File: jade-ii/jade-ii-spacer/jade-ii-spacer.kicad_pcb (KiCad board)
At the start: 2 copper layers, 93 x 127.3 mm, 23 parts

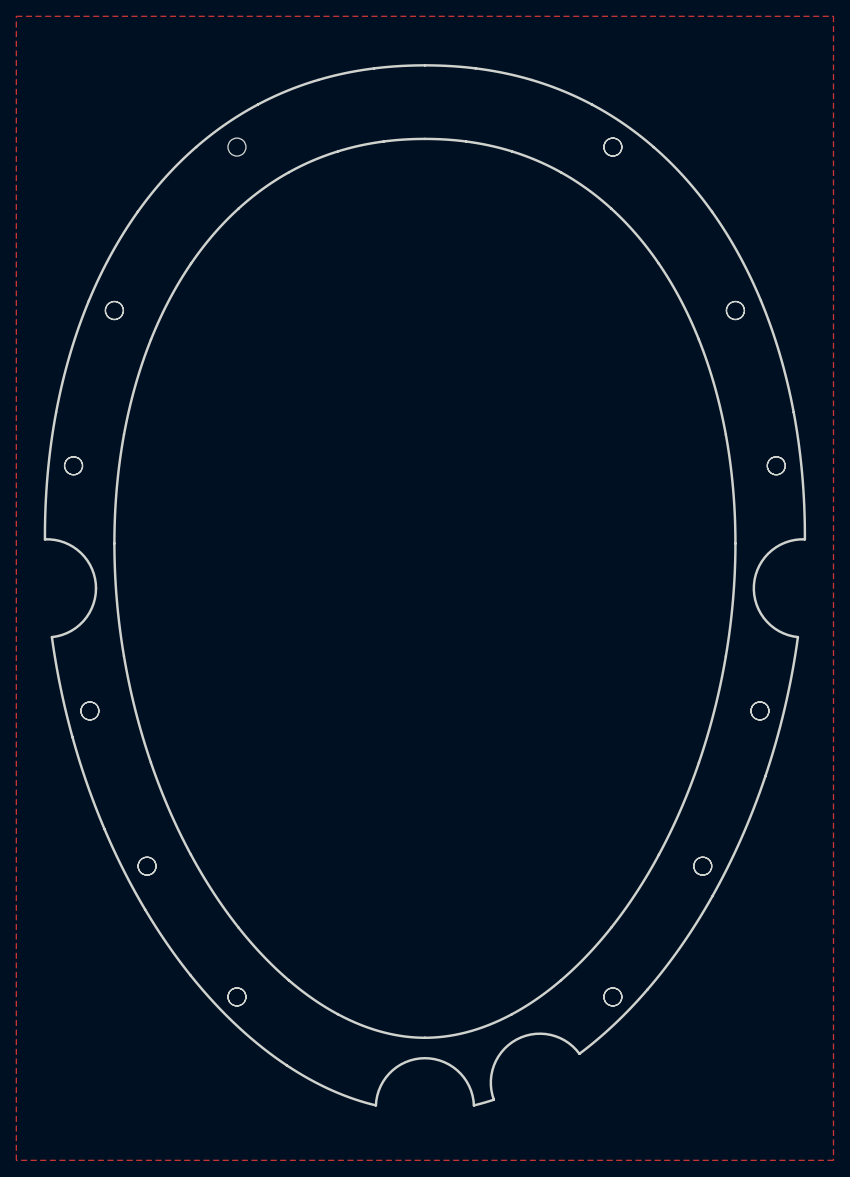
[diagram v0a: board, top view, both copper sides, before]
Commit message: jade: spacer should have 3 holes on the bottom
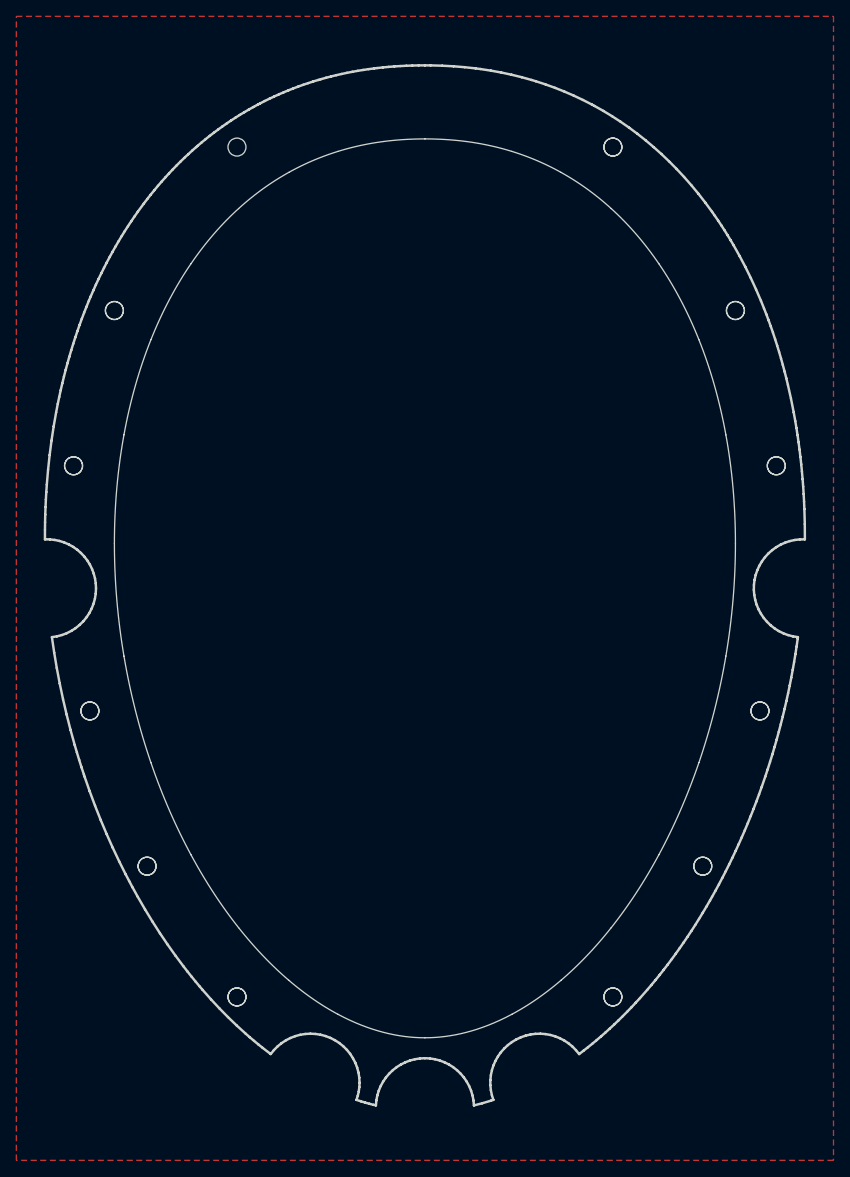
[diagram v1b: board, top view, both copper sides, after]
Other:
- outline, holes or cut-outs redrawn

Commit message: jade: remove top solder mask from spacer
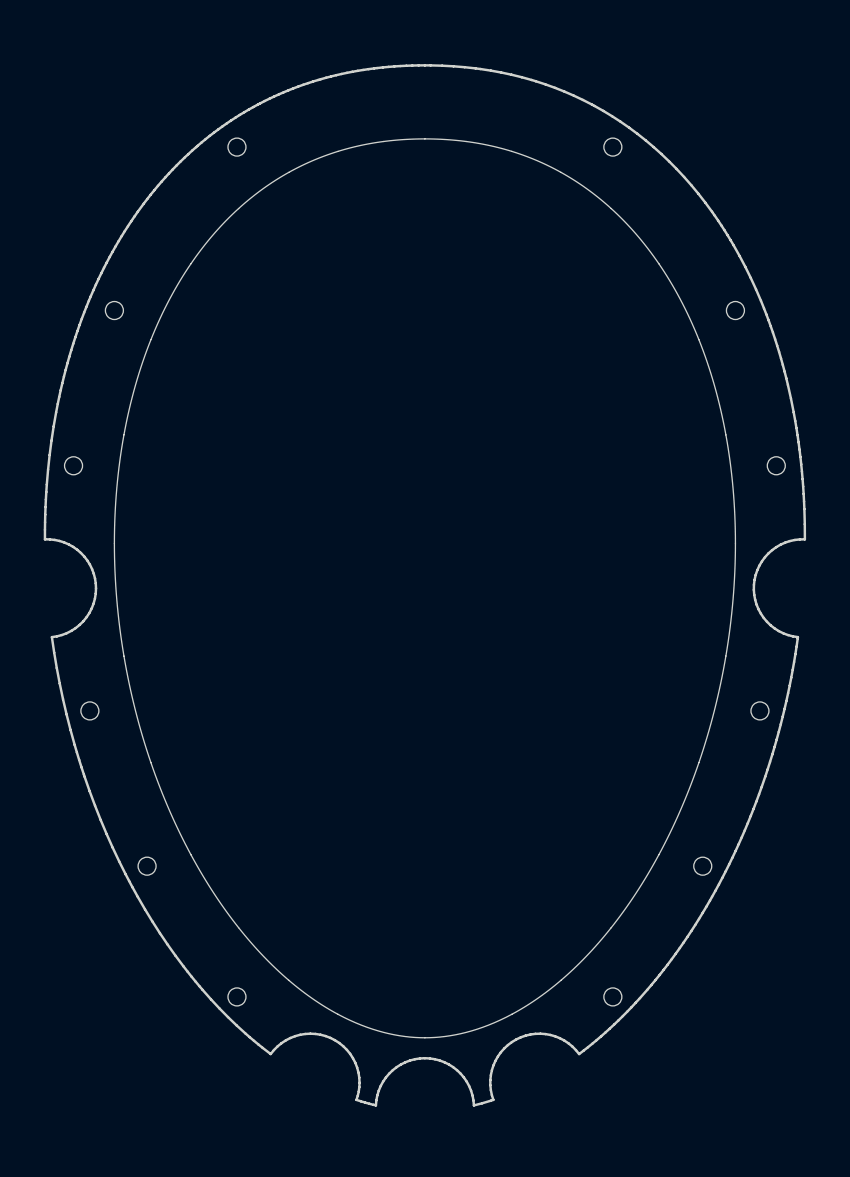
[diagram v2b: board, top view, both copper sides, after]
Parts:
- removed ? (x11): , 
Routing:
- removed copper zone on F.Cu, net (none)

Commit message: jade: i don't even know
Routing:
- added copper zone on F.Cu, net (none)
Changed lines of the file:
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@@
 		(layer "Edge.Cuts")
+	)
+	(zone
+		(net 0)
+		(net_name "")
+		(layer "F.Cu")
+		(hatch edge 0.5)
+		(connect_pads
+			(clearance 0.5)
+		)
+		(min_thickness 0.25)
+		(filled_areas_thickness no)
+		(fill yes
+			(thermal_gap 0.5)
+			(thermal_bridge_width 0.5)
+			(island_removal_mode 1)
+			(island_area_min 10)
+		)
+		(polygon
+			(pts
+				(xy -50 -70) (xy 50 -70) (xy 50 70) (xy -50 70)
+			)
+		)
 	)
 	(embedded_fonts no)

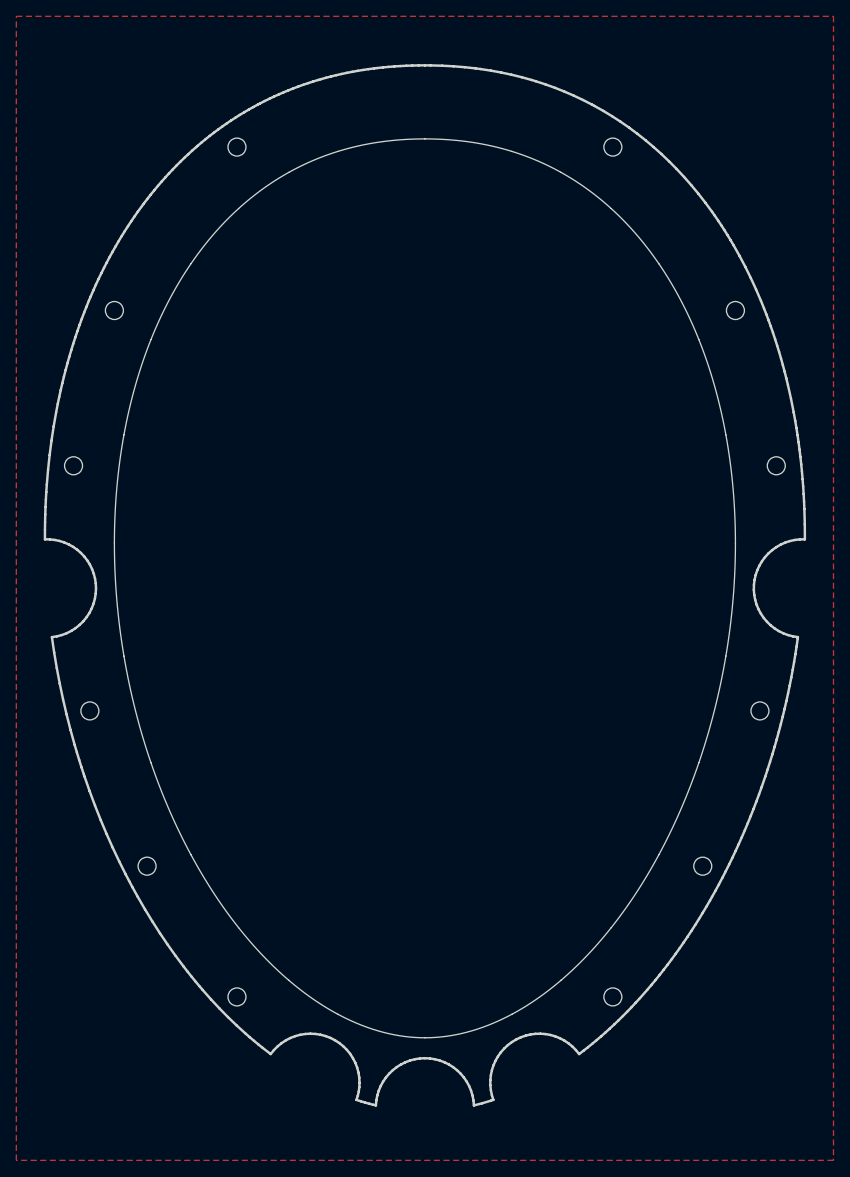
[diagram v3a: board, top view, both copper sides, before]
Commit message: jade: missing spacer cable solder point
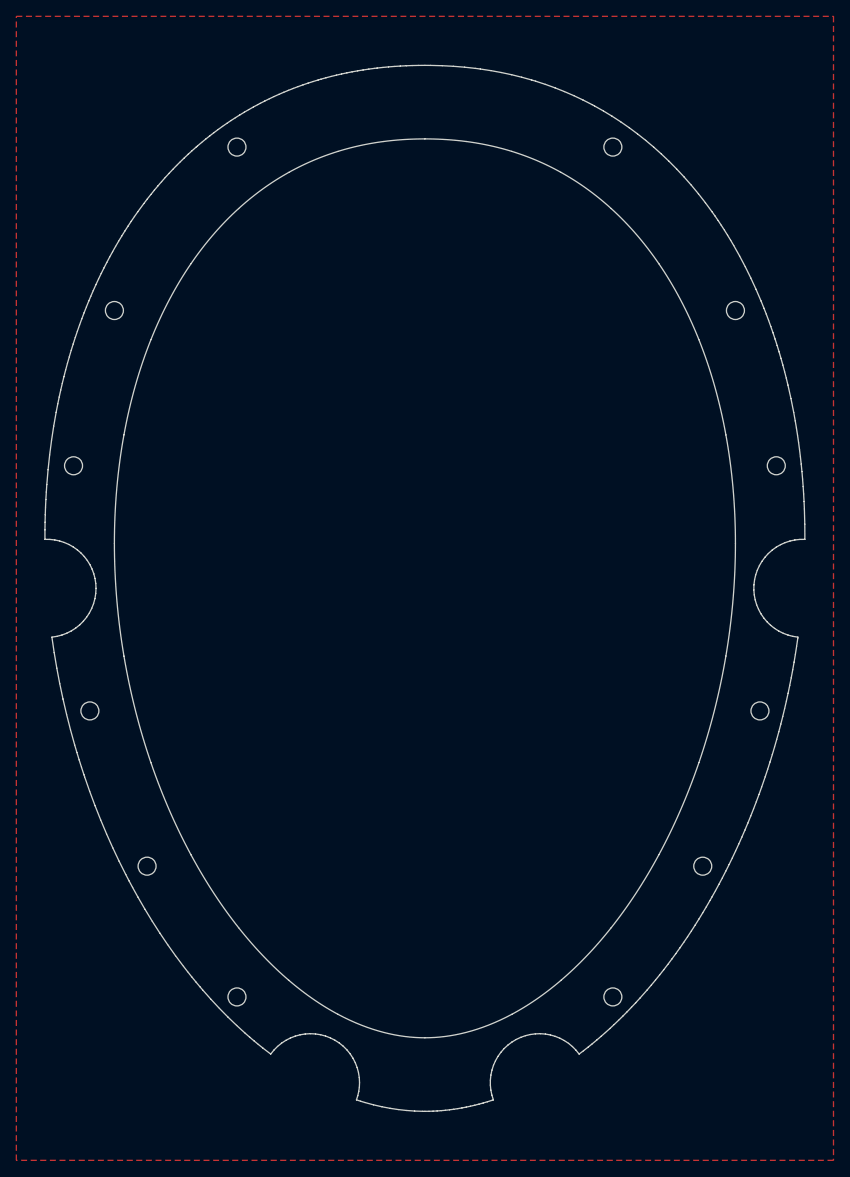
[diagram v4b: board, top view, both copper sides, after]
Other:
- board size 93 x 127.3 mm -> 93 x 128 mm
